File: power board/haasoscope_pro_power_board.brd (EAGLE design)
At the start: 72.4 x 97.5 mm, 94 parts, among them IC1 TPS5430DDAR, IC10 TPS5430DDAR, IC12 TPS7A7200RGTR, IC2 TPS5430DDAR, IC3 TPS7A7200RGTR, IC4 TPS5430DDAR, IC5 TPS72325DBVR, IC6 TPS5430DDAR, IC7 TPS7A7200RGTR, IC8 TPS5430DDAR, IC9 TPS7A7200RGTR, J1 2p-2.54, J10 2p-2.54, J11 2p-2.54, J13 2p-2.54, J2 2p-2.54, J3 2p-2.54, J4 2p-2.54, J5 2p-2.54, J6 2p-2.54, J7 2p-2.54, J8 2p-2.54, J9 2p-2.54

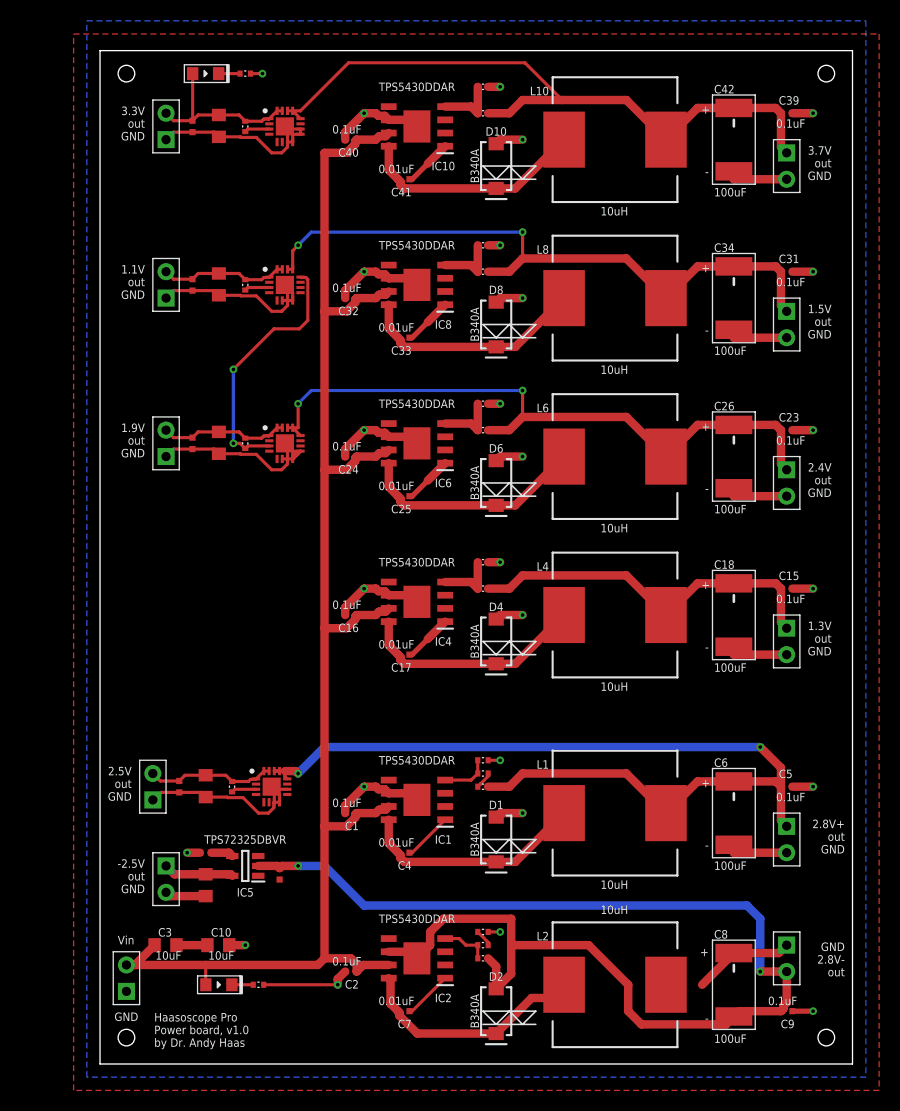
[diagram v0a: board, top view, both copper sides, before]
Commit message: 1.3->1.8 V for VLVDS
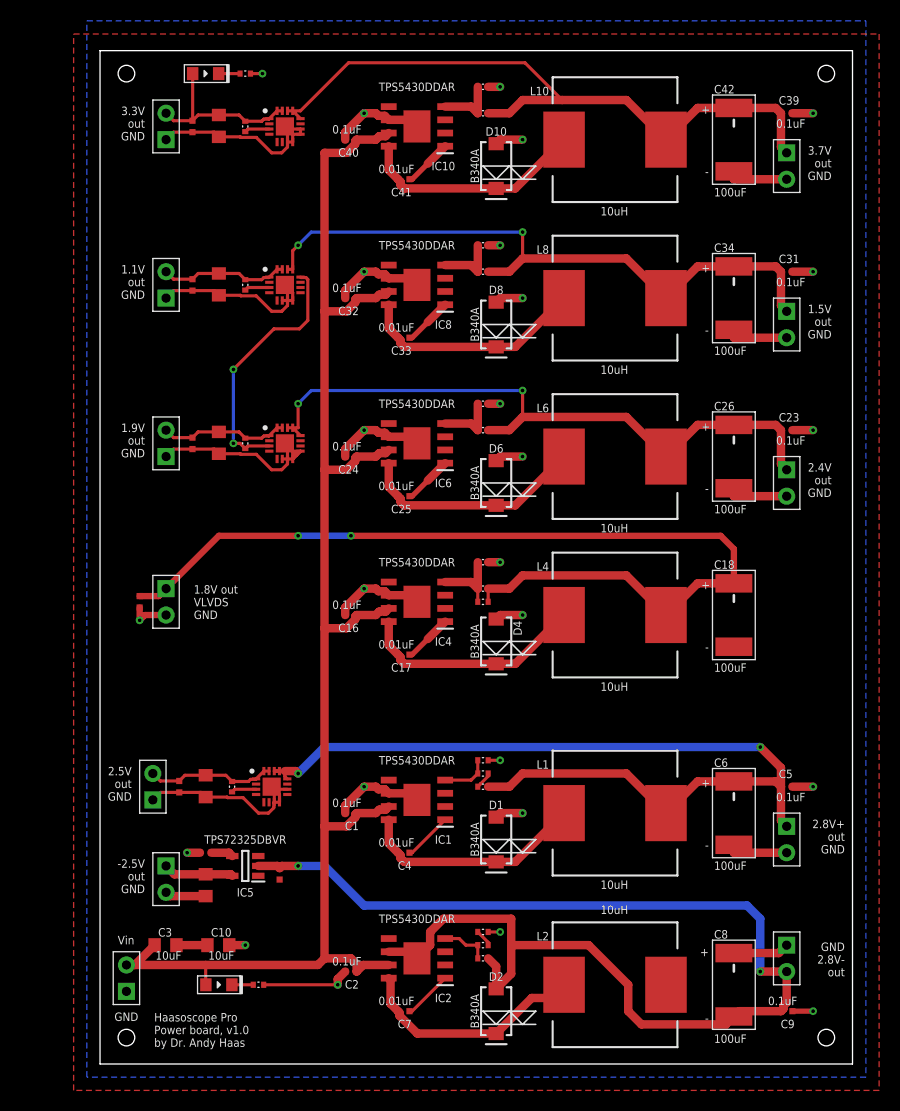
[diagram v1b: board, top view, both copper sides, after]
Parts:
- added R21: 10k, FlashPCB_Resistors:RES-0402
- R8: value 1k -> 10k
- moved C15 62.2 mm to (5.08, 45.7), turned to 270 degrees
- moved J5 59.8 mm to (7.62, 45.7)
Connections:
- removed net 1V3: C15.1, C18.+, J5.1, L4.2, R8.P$2
- new net 1V8: C15.1, C18.+, J5.1, L4.2, R21.P$2, R8.P$2
- net FB3: now also R21.P$1
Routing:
- net 1V8: track 0.00 -> 91.6 mm, vias 0 -> 2
- net 1V3: track 35.8 -> 0.00 mm
- net GND: track 209.1 -> 201.0 mm
- net FB3: track 5.94 -> 7.21 mm
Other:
- board text added: "1.8V out VLVDS GND"
- board text removed: "1.3V out GND"
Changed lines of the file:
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@@
 <wire x1="41.91" y1="5.08" x2="40.64" y2="6.35" width="0.1524" layer="21"/>
 <wire x1="38.1" y1="5.08" x2="43.18" y2="5.08" width="0.1524" layer="21"/>
-<text x="71.628" y="43.815" size="0.8128" layer="21" rot="R180">1.3V
-out
+<text x="10.287" y="44.069" size="0.8128" layer="21">1.8V out
+VLVDS
 GND</text>
 <text x="59.817" y="41.783" size="0.8128" layer="21" rot="R180">-</text>
@@
 <attribute name="JLC_ROTATION" value="180" x="39.37" y="41.91" size="1.778" layer="27" rot="R270" display="off"/>
 <attribute name="LCSC" value="C64982" x="39.37" y="41.91" size="1.778" layer="27" rot="R270" display="off"/>
-<attribute name="NAME" x="39.37" y="44.831" size="0.8128" layer="21" ratio="20" align="bottom-center"/>
+<attribute name="NAME" x="41.021" y="43.18" size="0.8128" layer="21" ratio="20" rot="R270" align="bottom-center"/>
 <attribute name="PROD_ID" value="DIO-09886" x="39.37" y="41.91" size="1.778" layer="27" rot="R270" display="off"/>
 <attribute name="VALUE" x="37.719" y="41.91" size="0.8128" layer="21" ratio="20" rot="R270" align="top-center"/>
 </element>
-<element name="J5" library="Seeed-Connector" library_urn="urn:adsk.eagle:library:478" package="H2-2.54" package3d_urn="urn:adsk.eagle:package:33132/1" value="2p-2.54" x="67.31" y="41.91" smashed="yes">
-<attribute name="MPN" value="P125-1102A0BS116A1" x="67.31" y="41.91" size="1.778" layer="27" display="off"/>
-</element>
-<element name="C15" library="Nordic_nRF" library_urn="urn:adsk.eagle:library:169009" package="RESC0402_N" package3d_urn="urn:adsk.eagle:package:2593732/1" value="0.1uF" x="67.31" y="46.99" smashed="yes">
-<attribute name="NAME" x="66.548" y="47.8155" size="0.8128" layer="21"/>
-<attribute name="VALUE" x="66.294" y="45.593" size="0.8128" layer="21"/>
-</element>
+<element name="J5" library="Seeed-Connector" library_urn="urn:adsk.eagle:library:478" package="H2-2.54" package3d_urn="urn:adsk.eagle:package:33132/1" value="2p-2.54" x="7.62" y="45.72" smashed="yes">
+<attribute name="MPN" value="P125-1102A0BS116A1" x="7.62" y="45.72" size="1.778" layer="27" display="off"/>
+</element>
+<element name="C15" library="Nordic_nRF" library_urn="urn:adsk.eagle:library:169009" package="RESC0402_N" package3d_urn="urn:adsk.eagle:package:2593732/1" value="0.1uF" x="5.08" y="45.72" smashed="yes" rot="R270"/>
 <element name="C16" library="Nordic_nRF" library_urn="urn:adsk.eagle:library:169009" package="RESC0402_N" package3d_urn="urn:adsk.eagle:package:2593732/1" value="0.1uF" x="25.4" y="44.45" smashed="yes" rot="R180">
 <attribute name="NAME" x="26.162" y="43.6245" size="0.8128" layer="21" rot="R180"/>
@@
 <attribute name="VALUE" x="31.75" y="49.53" size="0.8128" layer="21" rot="R180" align="center"/>
 </element>
-<element name="R8" library="FlashPCB_Resistors" package="RES-0402" value="1k" x="38.1" y="46.99" smashed="yes"/>
+<element name="R8" library="FlashPCB_Resistors" package="RES-0402" value="10k" x="38.1" y="46.99" smashed="yes"/>
 <element name="L6" library="SparkFun-Passives" package="CDRH125" value="10uH" x="50.8" y="59.69" smashed="yes" rot="R90">
 <attribute name="LCSC" value="C339970" x="50.8" y="59.69" size="1.778" layer="27" rot="R90" display="off"/>
@@
 </element>
 <element name="R18" library="FlashPCB_Resistors" package="RES-0402" value="3.3k" x="15.24" y="96.52" smashed="yes" rot="R180"/>
+<element name="R21" library="FlashPCB_Resistors" package="RES-0402" value="10k" x="38.1" y="45.72" smashed="yes"/>
 </elements>
 <signals>
@@
 <wire x1="24.13" y1="8.89" x2="24.13" y2="9.44" width="0.8128" layer="1"/>
 <wire x1="24.13" y1="9.44" x2="24.85" y2="10.16" width="0.8128" layer="1"/>
-<wire x1="59.182" y1="8.89" x2="62.23" y2="11.938" width="0.8128" layer="1"/>
 <wire x1="62.23" y1="11.938" x2="66.548" y2="11.938" width="0.8128" layer="1"/>
 <wire x1="66.548" y1="11.938" x2="67.31" y2="12.7" width="0.8128" layer="1"/>
@@
 <via x="26.67" y="46.99" extent="1-16" drill="0.35"/>
 <via x="41.91" y="44.45" extent="1-16" drill="0.35"/>
-<via x="69.85" y="46.99" extent="1-16" drill="0.35"/>
 <wire x1="26.67" y1="46.99" x2="24.85" y2="45.17" width="0.8128" layer="1"/>
 <wire x1="24.85" y1="45.17" x2="24.85" y2="44.45" width="0.8128" layer="1"/>
@@
 <wire x1="29.038" y1="46.355" x2="31.115" y2="46.355" width="0.8128" layer="1"/>
 <wire x1="31.115" y1="46.355" x2="31.75" y2="45.72" width="0.8128" layer="1"/>
-<wire x1="67.86" y1="46.99" x2="69.85" y2="46.99" width="0.8128" layer="1"/>
-<wire x1="67.31" y1="40.64" x2="62.23" y2="40.64" width="0.8128" layer="1"/>
-<wire x1="62.23" y1="40.64" x2="62.23" y2="41.402" width="0.8128" layer="1"/>
 <wire x1="39.37" y1="44.06" x2="39.76" y2="44.45" width="0.8128" layer="1"/>
 <wire x1="39.76" y1="44.45" x2="41.91" y2="44.45" width="0.8128" layer="1"/>
@@
 <via x="16.891" y="96.52" extent="1-16" drill="0.35"/>
 <wire x1="15.74" y1="96.52" x2="16.891" y2="96.52" width="0.3048" layer="1"/>
+<via x="5.08" y="43.942" extent="1-16" drill="0.35"/>
+<wire x1="5.08" y1="45.17" x2="5.08" y2="43.942" width="0.6096" layer="1"/>
+<wire x1="5.08" y1="43.942" x2="5.588" y2="44.45" width="0.6096" layer="1"/>
+<wire x1="5.588" y1="44.45" x2="7.62" y2="44.45" width="0.6096" layer="1"/>
 </signal>
 <signal name="2V8-">
@@
 <wire x1="36.965" y1="47.625" x2="37.6" y2="46.99" width="0.8128" layer="1"/>
 <wire x1="37.6" y1="46.99" x2="37.6" y2="49.53" width="0.8128" layer="1"/>
-</signal>
-<signal name="1V3">
+<contactref element="R21" pad="P$1"/>
+<wire x1="37.6" y1="46.99" x2="37.6" y2="45.72" width="0.3048" layer="1"/>
+</signal>
+<signal name="1V8">
 <contactref element="L4" pad="2"/>
 <contactref element="J5" pad="1"/>
@@
 <wire x1="62.23" y1="47.498" x2="58.748" y2="47.498" width="0.8128" layer="1"/>
 <wire x1="58.748" y1="47.498" x2="55.7" y2="44.45" width="0.8128" layer="1"/>
-<wire x1="62.23" y1="47.498" x2="66.252" y2="47.498" width="0.8128" layer="1"/>
-<wire x1="66.252" y1="47.498" x2="66.76" y2="46.99" width="0.8128" layer="1"/>
-<wire x1="66.76" y1="46.99" x2="66.76" y2="43.73" width="0.8128" layer="1"/>
-<wire x1="66.76" y1="43.73" x2="67.31" y2="43.18" width="0.8128" layer="1"/>
+<contactref element="R21" pad="P$2"/>
+<wire x1="38.6" y1="46.99" x2="38.6" y2="45.72" width="0.3048" layer="1"/>
+<wire x1="62.23" y1="47.498" x2="62.23" y2="50.8" width="0.6096" layer="1"/>
+<wire x1="62.23" y1="50.8" x2="60.96" y2="52.07" width="0.6096" layer="1"/>
+<via x="25.4" y="52.07" extent="1-16" drill="0.35"/>
+<wire x1="25.4" y1="52.07" x2="20.32" y2="52.07" width="0.6096" layer="16"/>
+<via x="20.32" y="52.07" extent="1-16" drill="0.35"/>
+<wire x1="20.32" y1="52.07" x2="12.7" y2="52.07" width="0.6096" layer="1"/>
+<wire x1="12.7" y1="52.07" x2="7.62" y2="46.99" width="0.6096" layer="1"/>
+<wire x1="60.96" y1="52.07" x2="25.4" y2="52.07" width="0.6096" layer="1"/>
+<wire x1="7.62" y1="46.99" x2="6.9" y2="46.27" width="0.6096" layer="1"/>
+<wire x1="6.9" y1="46.27" x2="5.08" y2="46.27" width="0.6096" layer="1"/>
 </signal>
 <signal name="SW4">

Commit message: add 2.5D for fpga, and add 1V9D for VLVDS
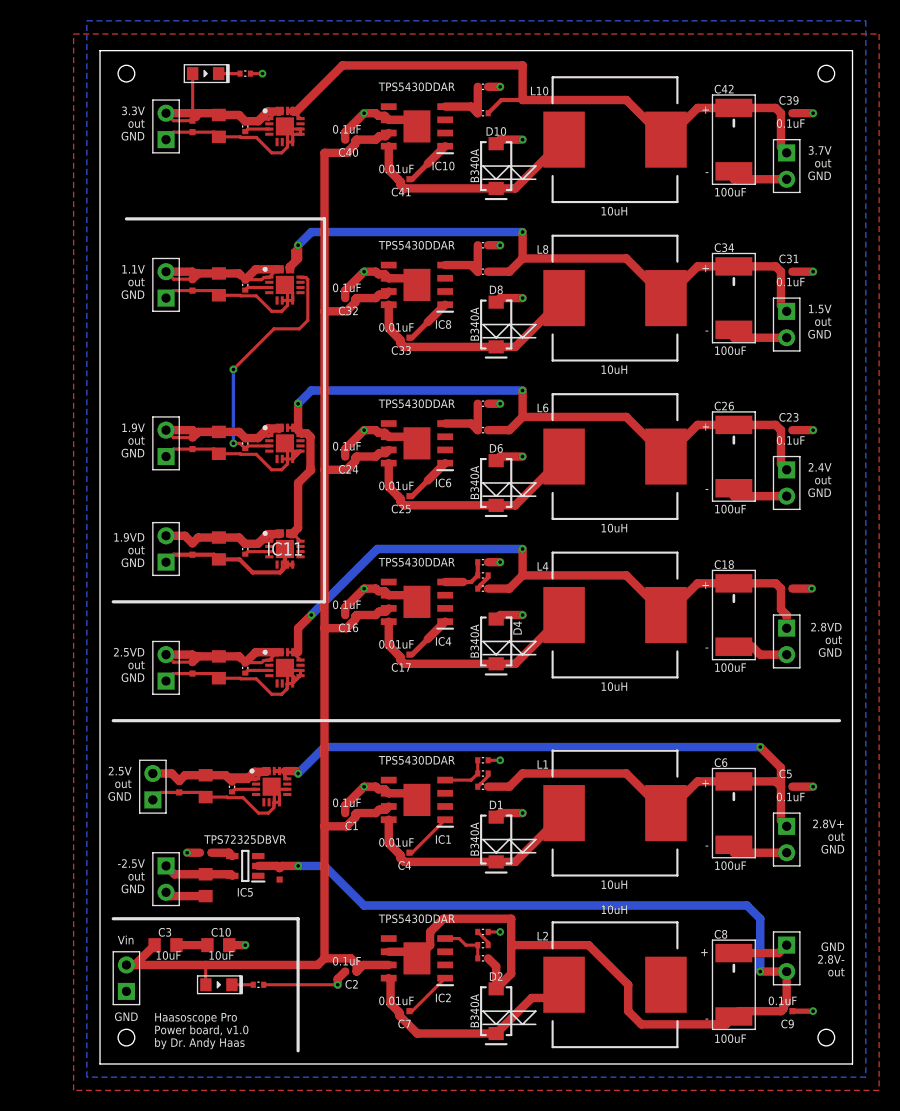
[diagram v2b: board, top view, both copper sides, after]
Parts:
- added C28, C38: 10uF, Nordic_nRF:RESC0805_N
- added C29, C43: 0.1uF, Nordic_nRF:RESC0402_N
- added IC11, IC14: TPS7A7200RGTR, TPS7A7200RGTR:QFN50P300X300X100-17N
- added J12, J15: 2p-2.54, Seeed-Connector:H2-2.54
- added R22, R24: 20k, FlashPCB_Resistors:RES-0402
- R8: value 10k -> 3.3k
- moved C15 62.2 mm to (67.3, 47.0), turned to 0 degrees
- moved J5 59.8 mm to (67.3, 41.9)
- moved R21 2.54 mm to (38.1, 48.3)
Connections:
- removed net 1V8: C15.1, C18.+, J5.1, L4.2, R21.P$2, R8.P$2
- new net 1V9DOUT: C28.1, C29.1, IC11.1, IC11.15, IC11.16, J12.2, R22.P$1
- new net 2V5DOUT: C38.1, C43.1, IC14.1, IC14.15, IC14.16, J15.2, R24.P$1
- new net 2V8D: C15.1, C18.+, IC14.12, IC14.13, IC14.14, J5.1, L4.2, R8.P$2
- new net N$7: R21.P$2, R8.P$1
- new net PG1V9D: IC11.3, R22.P$2
- new net PG2V5D: IC14.3, R24.P$2
- net 2V4: now also IC11.12, IC11.13, IC11.14
- net FB3: no longer R8.P$1
- net GND: now also C28.2, C29.2, C38.2, C43.2, IC11.17, IC11.6, IC11.7, IC11.8, IC11.9, IC14.10, IC14.17, IC14.7, IC14.8, IC14.9, J12.1, J15.1
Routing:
- net 1V8: track 91.6 -> 0.00 mm, vias 2 -> 0
- net 2V8D: track 0.00 -> 67.5 mm, vias 0 -> 2
- net GND: track 201.0 -> 241.4 mm
- net 2V4: track 64.8 -> 87.8 mm
- net 2V5DOUT: track 0.00 -> 20.0 mm
- net 1V9DOUT: track 0.00 -> 16.1 mm
- net 3V3OUT: track 16.9 -> 26.3 mm
- net 1V9OUT: track 12.4 -> 20.0 mm
- net 1V1OUT: track 12.4 -> 19.9 mm
- net 2V5OUT: track 12.4 -> 16.4 mm
- net 1V5: track 63.5 -> 66.1 mm
- net FB3: track 7.21 -> 4.67 mm
- net PG2V5D: track 0.00 -> 2.41 mm
- net PG1V9D: track 0.00 -> 2.41 mm
- net 3V7: track 66.7 -> 64.6 mm
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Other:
- board text added: "1.9VD out GND"
- board text added: "2.5VD out GND"
- board text added: "2.8VD out GND"
- board text removed: "1.8V out VLVDS GND"
